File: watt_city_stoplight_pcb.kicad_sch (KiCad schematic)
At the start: 0 parts

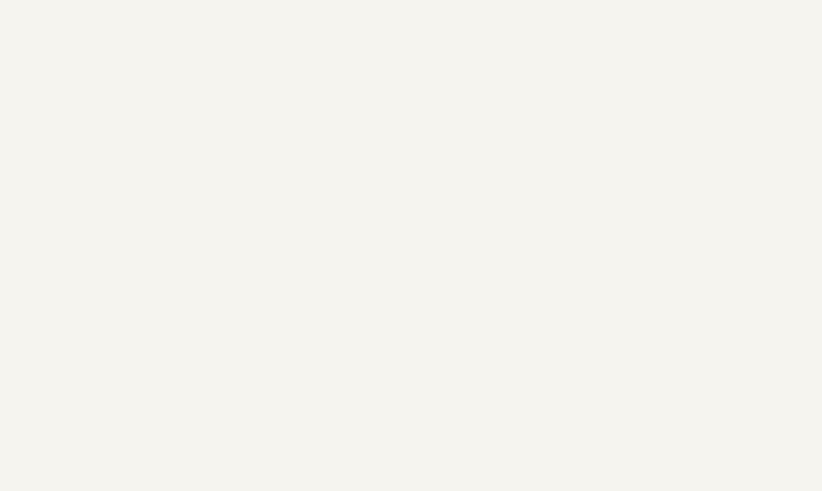
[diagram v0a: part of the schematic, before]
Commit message: added button pullup + mounting holes
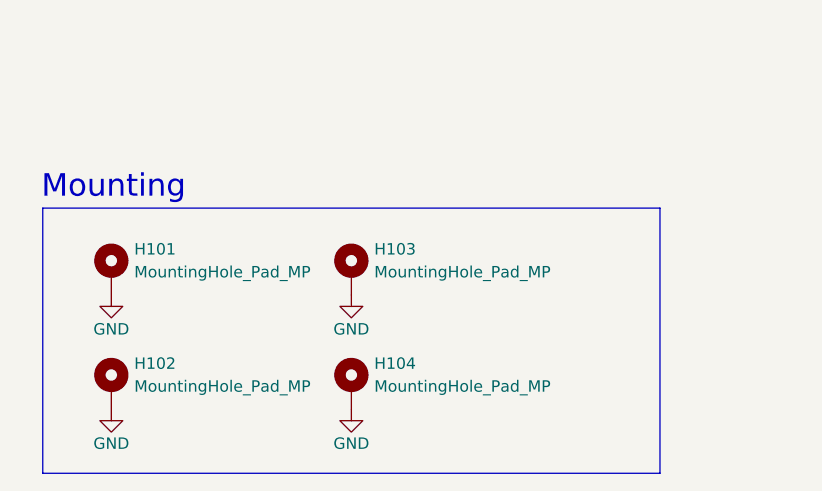
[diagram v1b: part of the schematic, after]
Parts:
- added H101, H102, H103, H104: MountingHole_Pad_MP, MountingHole:MountingHole_2.7mm_M2.5_Pad_Via, symbol Mechanical:MountingHole_Pad
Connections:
- new net GND: H101.1, H102.1, H103.1, H104.1
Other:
- note added: "Mounting"
